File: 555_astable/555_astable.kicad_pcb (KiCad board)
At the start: 2 copper layers, 43 x 32.9 mm, 13 parts, among them J1 Conn_01x02, J2 Conn_01x03, SW1 SW_SPST, U1 NE555P

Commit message: actualizar 555 oficial
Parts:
- removed the REF** at (107.8, 38.8)
- removed the REF** at (107.8, 66.5)
- added J3: Conn_01x02, TerminalBlock:TerminalBlock_MaiXu_MX126-5.0-02P_1x02_P5.00mm, F.Cu at (104.7, 64.2)
- SW1: footprint Button_Switch_THT:SW_CK_JS202011CQN_DPDT_Straight -> Button_Switch_THT:SW_E-Switch_EG1271_SPDT
- moved R2 9.67 mm to (88.2, 62.5)
- moved J2 3.19 mm to (104.8, 52.2)
- moved C2 3.00 mm to (84.0, 64.2), turned to 90 degrees
- moved C1 1.25 mm to (83.2, 52.8)
- moved REF** 0.25 mm to (69.8, 38.5)
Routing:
- net Net-(J2-Pin_2): track 42.0 -> 55.8 mm
- net VCC: track 39.8 -> 51.6 mm
- net Net-(U1-CONT): track 7.80 -> 12.7 mm
- net Net-(J2-Pin_3): track 47.4 -> 45.9 mm
- net GND: track 0.00 -> 1.06 mm
- net Net-(J2-Pin_1): track 23.6 -> 24.2 mm
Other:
- board size 43 x 32.9 mm -> 43 x 33 mm
- board text added: "555"
- board text added: "astable"
- board text added: "hecho x mateo arce"
- board text removed: "555-astable | hecho x mateo arce"

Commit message: fix 555 + design 4017
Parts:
- moved J3 17.0 mm to (104.2, 47.2)
- moved J2 12.1 mm to (104.3, 64.3)
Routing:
- net Net-(J2-Pin_2): track 55.8 -> 19.7 mm
- net Net-(U1-CONT): track 12.7 -> 35.1 mm
- net VCC: track 51.6 -> 68.4 mm
- net Net-(J2-Pin_1): track 24.2 -> 33.0 mm
- net Net-(J2-Pin_3): track 45.9 -> 51.9 mm
- net GND: track 1.06 -> 0.00 mm
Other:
- board text added: "2"
- board text added: "7"
- board text added: "gnd"
- board text added: "out"
- board text added: "pot"
- board text added: "vcc"

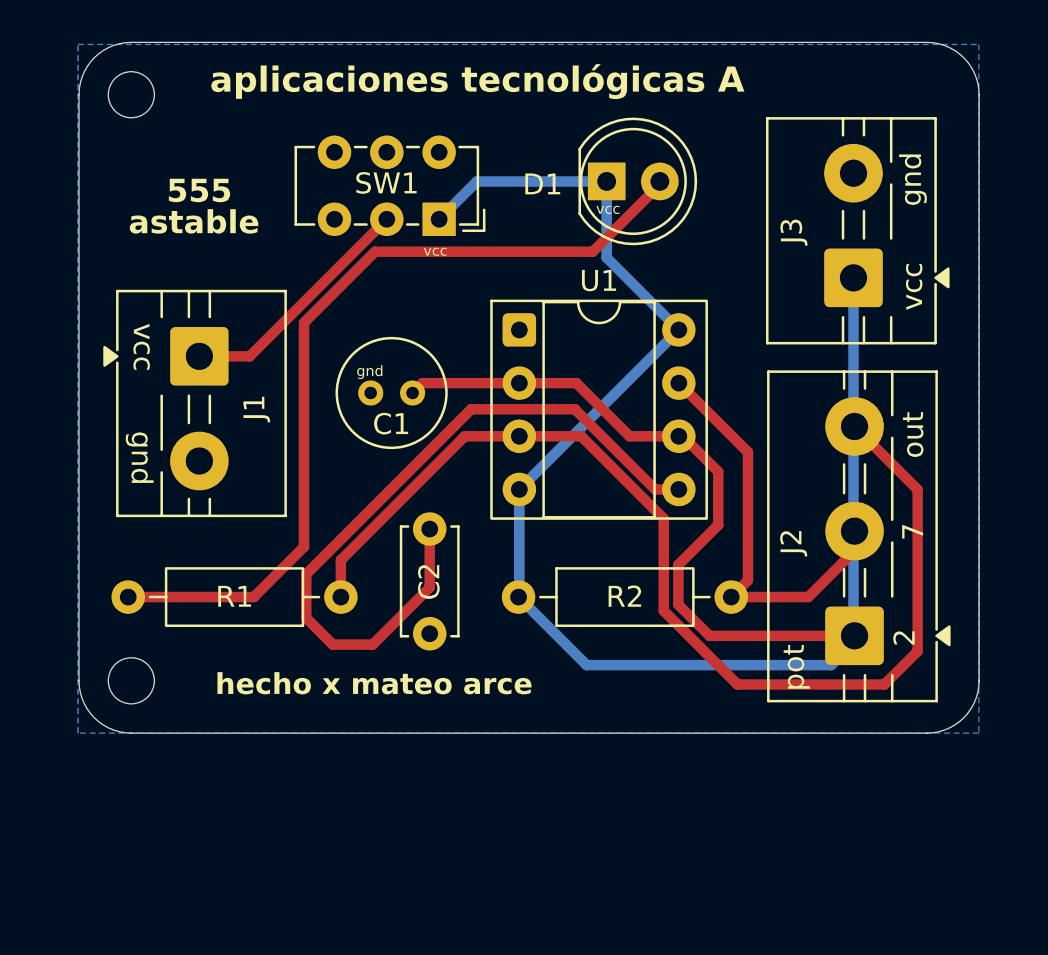
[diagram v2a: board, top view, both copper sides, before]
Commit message: nuevas footprints y pcb
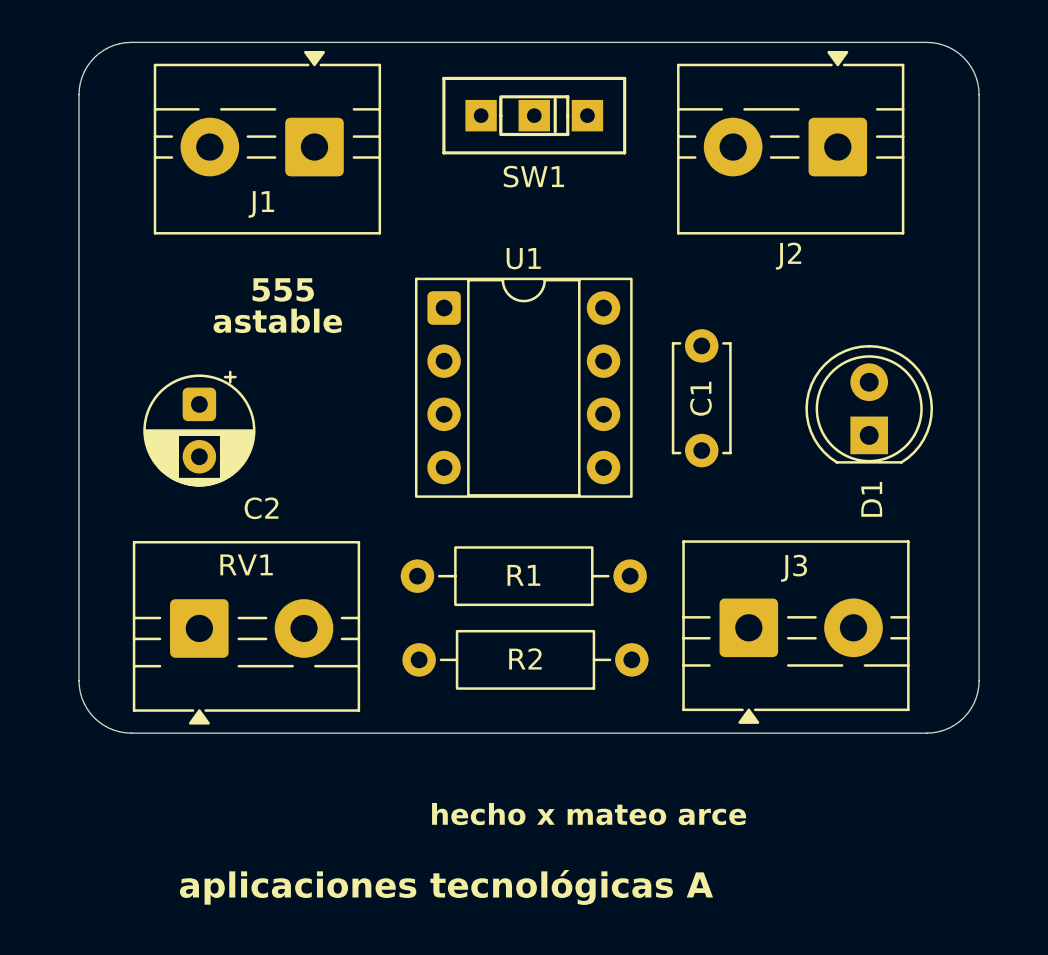
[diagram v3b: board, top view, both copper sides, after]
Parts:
- removed REF** (x2): MountingHole_2.2mm_M2, MountingHole:MountingHole_2.2mm_M2
- added RV1: 100k, TerminalBlock:TerminalBlock_MaiXu_MX126-5.0-02P_1x02_P5.00mm, F.Cu at (73.0, 64.0)
- C1: value 10uf -> 100n; footprint Capacitor_THT:C_Radial_D5.0mm_H5.0mm_P2.00mm -> Capacitor_THT:C_Disc_D5.0mm_W2.5mm_P5.00mm
- C2: value 100n -> 10uf; footprint Capacitor_THT:C_Disc_D5.0mm_W2.5mm_P5.00mm -> Capacitor_THT:CP_Radial_D5.0mm_P2.50mm
- J2: value Conn_01x03 -> Conn_01x02; footprint TerminalBlock:TerminalBlock_MaiXu_MX126-5.0-03P_1x03_P5.00mm -> TerminalBlock:TerminalBlock_MaiXu_MX126-5.0-02P_1x02_P5.00mm
- SW1: value SW_SPST -> SW_SPDT; footprint Button_Switch_THT:SW_E-Switch_EG1271_SPDT -> parla:spdt_ssd12d00g3
- moved J2 23.4 mm to (103.5, 41.0), turned to 180 degrees
- moved J3 17.4 mm to (99.2, 64.0), turned to 0 degrees
- moved D1 17.4 mm to (105.0, 54.8), turned to 90 degrees
- moved C2 15.5 mm to (73.0, 53.3), turned to -90 degrees
- moved C1 14.0 mm to (97.0, 50.5), turned to -90 degrees
- moved R1 13.9 mm to (93.6, 61.5)
- moved J1 11.4 mm to (78.5, 41.0), turned to 180 degrees
- moved SW1 6.72 mm to (89.0, 39.5)
- moved R2 6.19 mm to (93.7, 65.5), turned to 180 degrees
- moved U1 3.75 mm to (84.7, 48.7)
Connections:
- C1 pad 1: Net-(J2-Pin_1) -> GND
- C1 pad 2: GND -> Net-(U1-CONT)
- C2 pad 1: GND -> Net-(U1-THRES)
- C2 pad 2: Net-(U1-CONT) -> GND
- D1 pad 1: VCC -> GND
- J2 pad 1: Net-(J2-Pin_1) -> VCC
- J2 pad 2: Net-(J2-Pin_2) -> GND
- J3 pad 1: VCC -> Net-(J3-Pin_1)
- R1 pad 1: Net-(J2-Pin_3) -> Net-(U1-DISCH)
- R1 pad 2: Net-(D1-A) -> VCC
- R2 pad 1: VCC -> Net-(D1-A)
- R2 pad 2: Net-(J2-Pin_2) -> Net-(J3-Pin_1)
- SW1 pad 1: VCC -> unconnected-(SW1-A-Pad1)
- SW1 pad 2: Net-(J1-Pin_1) -> VCC
- SW1 pad 3: (no net) -> Net-(J1-Pin_1)
- U1 pad 2: Net-(J2-Pin_1) -> Net-(U1-THRES)
- U1 pad 3: Net-(J2-Pin_3) -> Net-(J3-Pin_1)
- U1 pad 6: Net-(J2-Pin_1) -> Net-(U1-THRES)
- U1 pad 7: Net-(J2-Pin_2) -> Net-(U1-DISCH)
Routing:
- net VCC: track 68.4 -> 0.00 mm
- net Net-(J2-Pin_3): track 51.9 -> 0.00 mm
- net Net-(D1-A): track 40.0 -> 0.00 mm
- net Net-(U1-CONT): track 35.1 -> 0.00 mm
- net Net-(J2-Pin_1): track 33.0 -> 0.00 mm
- net Net-(J2-Pin_2): track 19.7 -> 0.00 mm
- net Net-(J1-Pin_1): track 11.7 -> 0.00 mm
- removed copper zone on B.Cu, net GND
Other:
- board text removed: "2"
- board text removed: "7"
- board text removed: "gnd"
- board text removed: "out"
- board text removed: "pot"
- board text removed: "vcc"

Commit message: gerbers + correcciones
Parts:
- moved C2 4.04 mm to (77.0, 52.8)
- moved J1 3.67 mm to (77.5, 44.5)
- moved J2 3.54 mm to (103.8, 44.5)
- moved SW1 2.80 mm to (88.5, 42.2)
- moved D1 1.40 mm to (104.0, 55.8)
- moved C1 1.27 mm to (96.8, 51.8)
- moved R2 0.54 mm to (93.5, 66.0)
- moved R1 0.28 mm to (93.5, 61.2)
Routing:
- net Net-(U1-DISCH): track 0.00 -> 39.7 mm
- net VCC: track 0.00 -> 37.5 mm
- net Net-(J3-Pin_1): track 0.00 -> 31.1 mm
- net Net-(U1-THRES): track 0.00 -> 30.9 mm
- net Net-(D1-A): track 0.00 -> 29.3 mm
- net Net-(J1-Pin_1): track 0.00 -> 9.41 mm
- net Net-(U1-CONT): track 0.00 -> 4.62 mm
- added copper zone on B.Cu, net GND
- added copper zone on F.Cu, net GND
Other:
- board size 43 x 33 mm -> 46 x 29.5 mm
- board text added: "hecho por mateo arce"
- board text removed: "aplicaciones tecnológicas A"
- board text removed: "hecho x mateo arce"

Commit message: actualizar gerber
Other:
- board size 46 x 29.5 mm -> 42.9 x 29.5 mm
- board text added: "aplicaciones tecnológicas A"

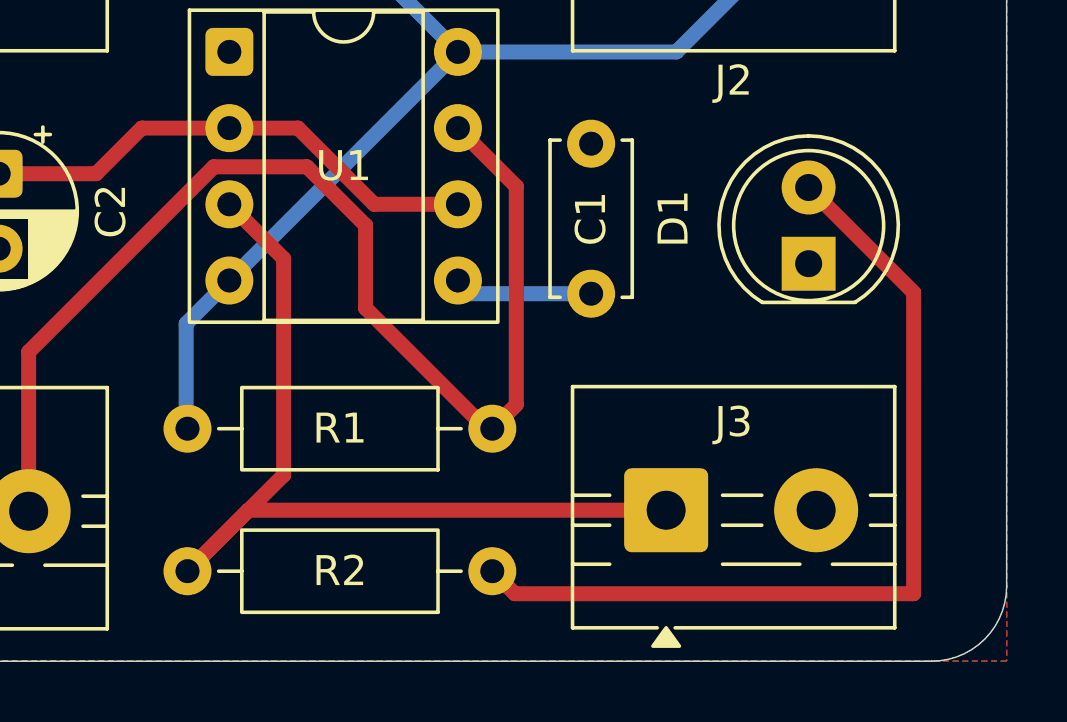
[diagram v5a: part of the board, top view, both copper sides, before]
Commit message: Update 555 board and add 4017 test design
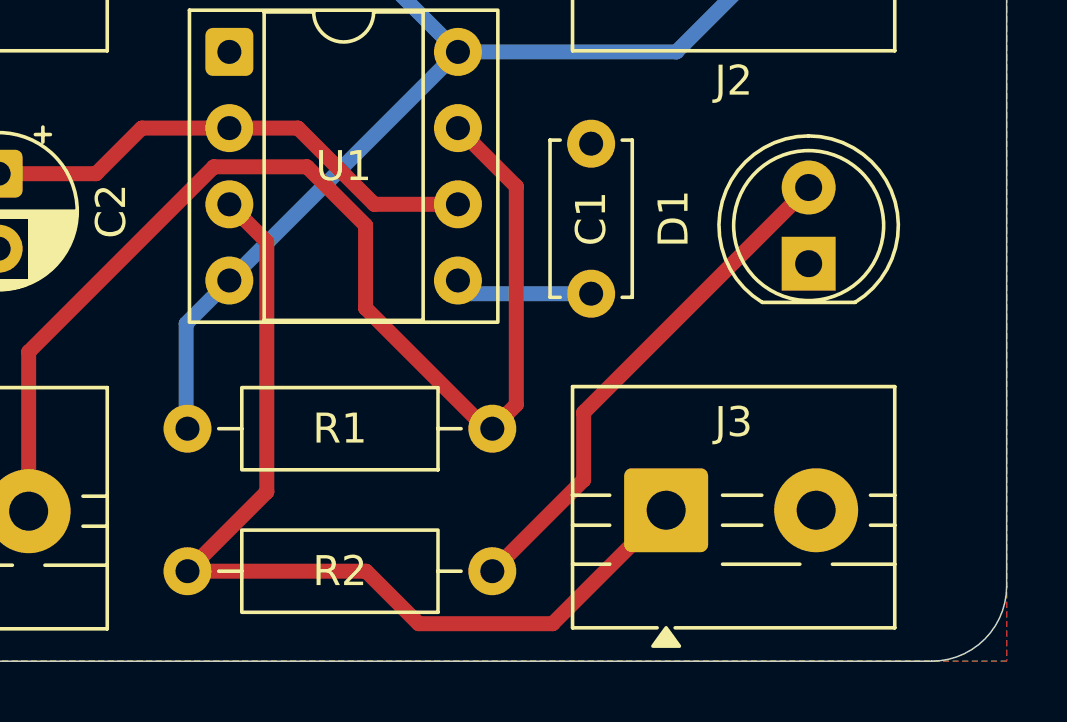
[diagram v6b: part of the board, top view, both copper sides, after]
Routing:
- net Net-(D1-A): track 29.3 -> 17.2 mm
- net Net-(J3-Pin_1): track 31.1 -> 32.1 mm
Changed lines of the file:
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@@
 	)
 	(segment
-		(start 85.3275 63.9675)
+		(start 85.94 63.355)
 		(end 83.295 66)
 		(width 0.5)
@@
 	)
 	(segment
-		(start 83.295 66)
-		(end 86.5 62.795)
+		(start 84.69 53.77)
+		(end 85.94 55.02)
 		(width 0.5)
 		(layer "F.Cu")
@@
 	)
 	(segment
-		(start 86.5 62.795)
-		(end 86.5 55.58)
+		(start 83.295 66)
+		(end 89.25 66)
 		(width 0.5)
 		(layer "F.Cu")
@@
 	)
 	(segment
-		(start 99.25 63.9675)
-		(end 85.3275 63.9675)
+		(start 89.25 66)
+		(end 91 67.75)
 		(width 0.5)
 		(layer "F.Cu")
@@
 	)
 	(segment
-		(start 86.5 55.58)
-		(end 84.69 53.77)
+		(start 91 67.75)
+		(end 95.4675 67.75)
+		(width 0.5)
+		(layer "F.Cu")
+		(net "Net-(J3-Pin_1)")
+	)
+	(segment
+		(start 85.94 55.02)
+		(end 85.94 63.355)
+		(width 0.5)
+		(layer "F.Cu")
+		(net "Net-(J3-Pin_1)")
+	)
+	(segment
+		(start 95.4675 67.75)
+		(end 99.25 63.9675)
 		(width 0.5)
 		(layer "F.Cu")
@@
 	)
 	(segment
-		(start 107.5 66.75)
-		(end 107.5 56.71)
-		(width 0.5)
-		(layer "F.Cu")
-		(net "Net-(D1-A)")
-	)
-	(segment
-		(start 94.205 66.75)
-		(end 107.5 66.75)
-		(width 0.5)
-		(layer "F.Cu")
-		(net "Net-(D1-A)")
-	)
-	(segment
-		(start 107.5 56.71)
-		(end 104 53.21)
+		(start 96.5 62.955)
+		(end 96.5 60.71)
 		(width 0.5)
 		(layer "F.Cu")
@@
 	(segment
 		(start 93.455 66)
-		(end 94.205 66.75)
+		(end 96.5 62.955)
 		(width 0.5)
 		(layer "F.Cu")
+		(net "Net-(D1-A)")
+	)
+	(segment
+		(start 96.5 60.71)
+		(end 104 53.21)
+		(width 0.5)
+		(layer "F.Cu")
